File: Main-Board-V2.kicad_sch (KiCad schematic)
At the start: 17 parts, among them IC2 REG1117-5, J1 776280-1, J2 BCS-114-L-S-PE-BE, J3 BCS-114-L-S-PE-BE, J4 776280-1, U4 ADM3057EBRWZ

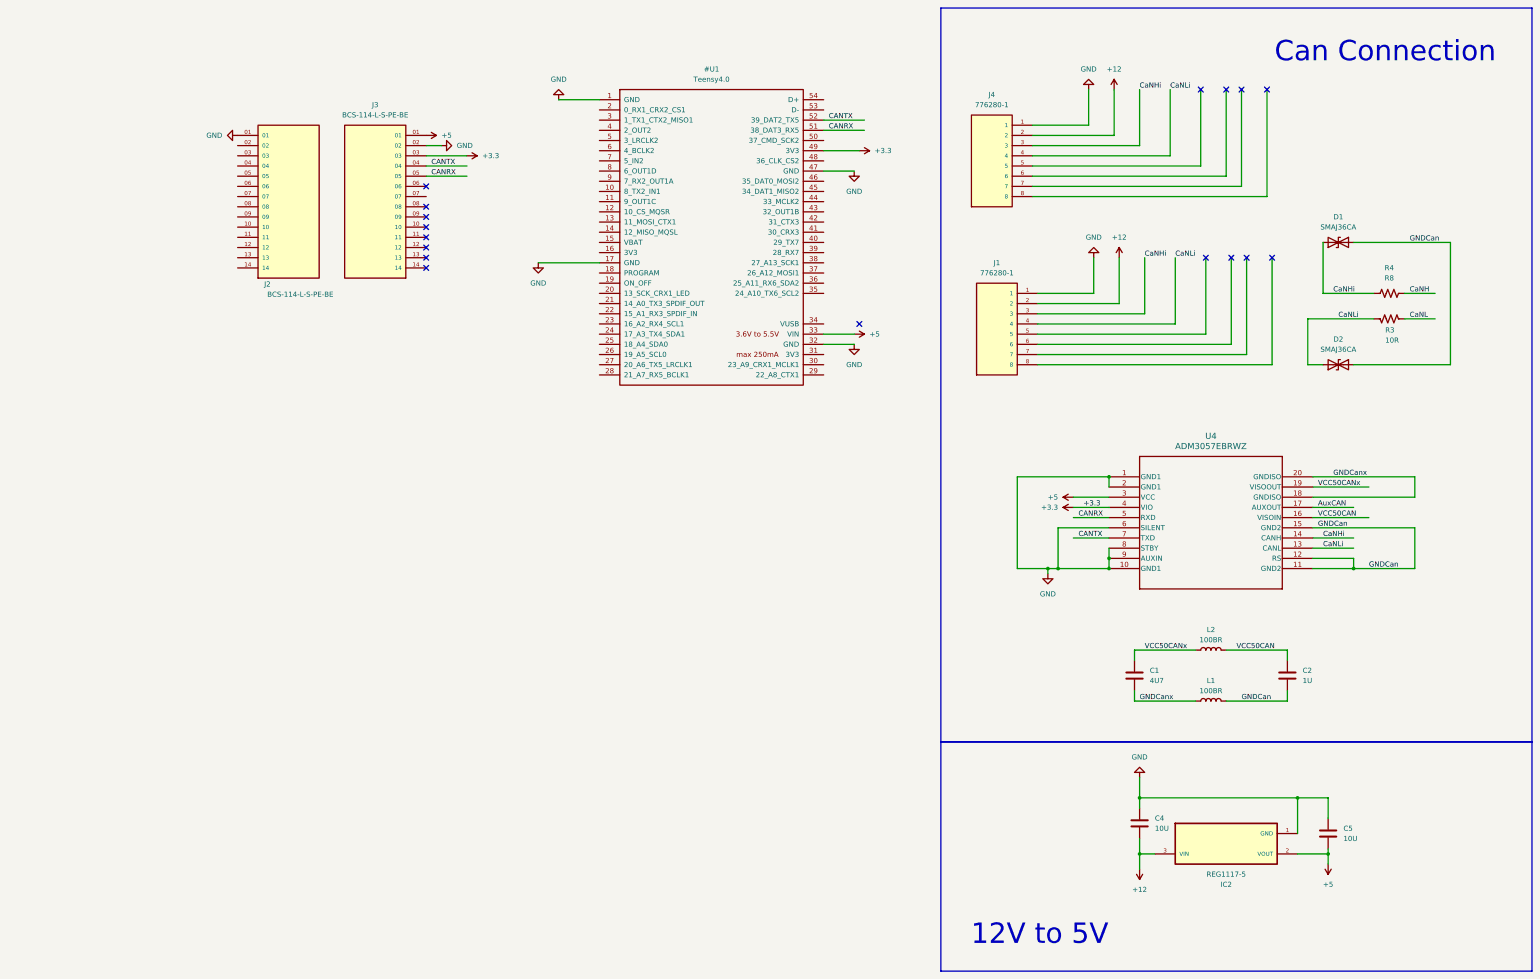
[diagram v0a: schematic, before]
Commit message: Seperated into sub sheets
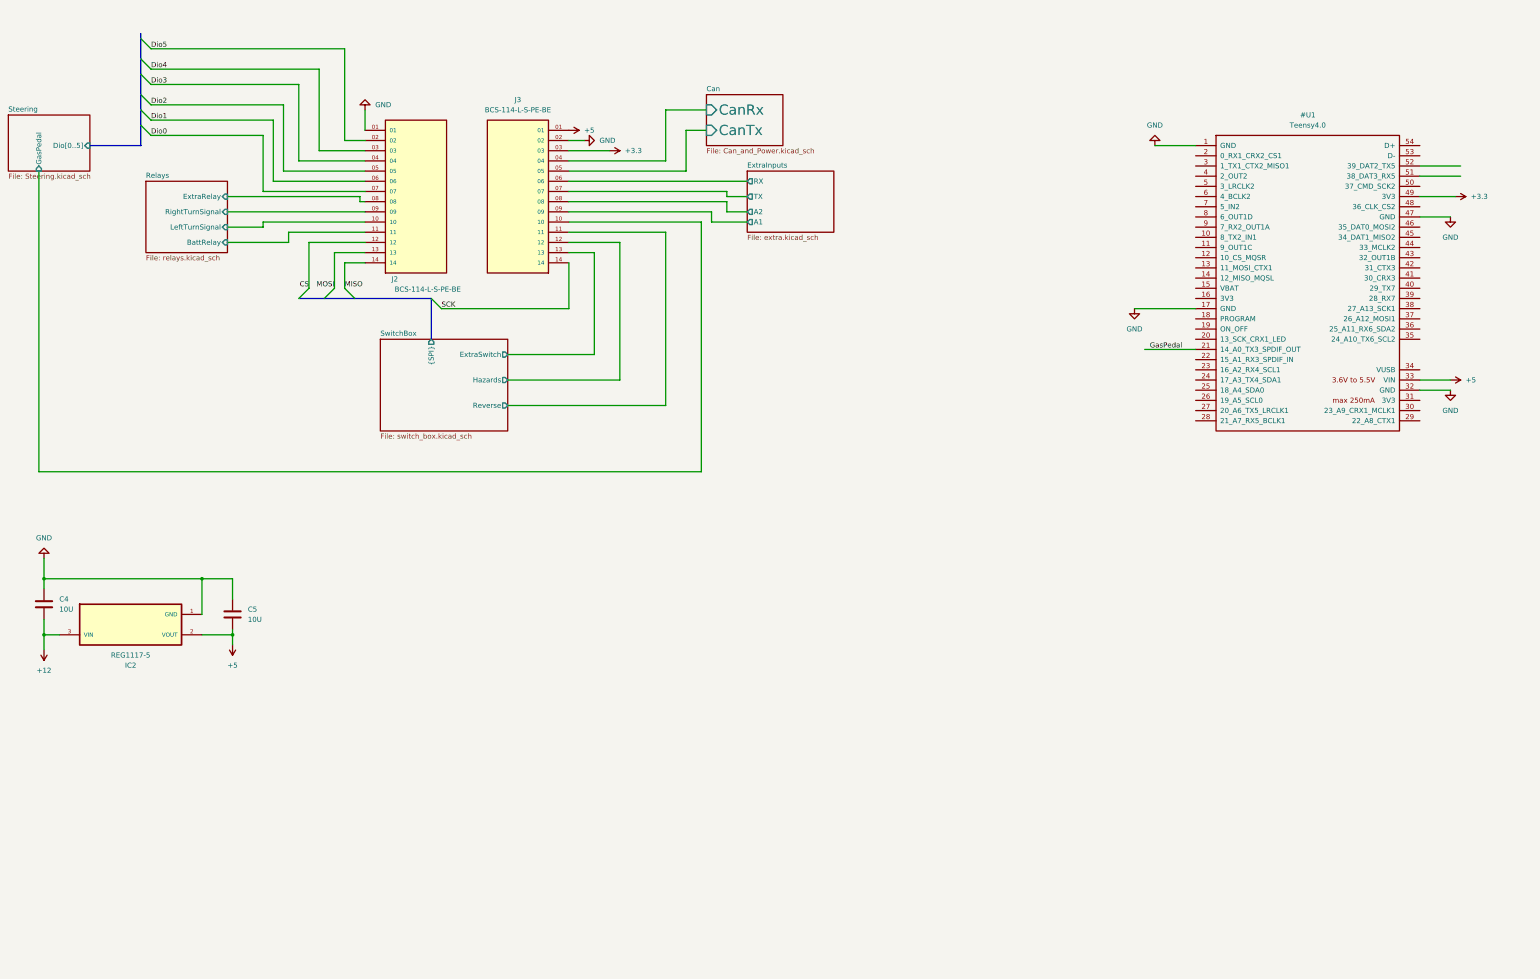
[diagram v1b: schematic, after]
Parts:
- removed C1: 4U7, GRM188R61E475KE11D:CAPC1608X95N, symbol Device:C
- removed C2: 1U, GRT155C80J105KE01J:CAPC1005X55N, symbol Device:C
- removed D1, D2: SMAJ36CA, SMAJ36CA:SMASERIES-M, symbol Diode:SMAJ36CA
- removed J1, J4: 776280-1, 776280-1:TE_776280-1, symbol 776280-1:776280-1
- removed L1, L2: 100BR, RN73C2B100RBTDF:RESC3015X65N, symbol Device:L
- removed R3: 10R, Resistor_SMD:R_0603_1608Metric, symbol Device:R_US
- removed R4: R8, Resistor_SMD:R_0603_1608Metric, symbol Device:R_US
- removed U4: ADM3057EBRWZ, ADM3057EBRWZ:SOIC127P1032X265-20N, symbol 2025-07-12_07-19-05:ADM3057EBRWZ
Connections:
- net Dio5: now reaches J2.02
- net Dio4: now reaches J2.03
- net Dio3: now reaches J2.04
- net Dio2: now reaches J2.05
- net Dio1: now reaches J2.06
- net Dio0: now reaches J2.07
- net Relays/ExtraRelay: now reaches J2.08
- net Relays/RightTurnSignal: now reaches J2.09
- net Relays/LeftTurnSignal: now reaches J2.10
- net Relays/BattRelay: now reaches J2.11
- net CS: now reaches J2.12
- net MOSI: now reaches J2.13
- net MISO: now reaches J2.14
- net GasPedal: now reaches #U1.21 (14_A0_TX3_SPDIF_OUT)
- net ExtraInputs/RX: now reaches J3.06
- net ExtraInputs/TX: now reaches J3.07
- net ExtraInputs/A2: now reaches J3.08
- net ExtraInputs/A1: now reaches J3.09
- net Steering/GasPedal: now reaches J3.10
- net SwitchBox/Reverse: now reaches J3.11
- net SwitchBox/Hazards: now reaches J3.12
- net SwitchBox/ExtraSwitch: now reaches J3.13
- net SCK: now reaches J3.14
- net CANRX: no longer names the net of #U1.51 (38_DAT3_RX5)
- net CANRX: no longer J3.05
- net CANTX: no longer names the net of #U1.52 (39_DAT2_TX5)
- net CANTX: no longer J3.04
- new net Can/CanRx: J3.04
- new net Can/CanTx: J3.05
- no-connect marks 17 -> 0
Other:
- added sheet Can (Can_and_Power.kicad_sch)
- added sheet ExtraInputs (extra.kicad_sch)
- added sheet Relays (relays.kicad_sch)
- added sheet Steering (Steering.kicad_sch)
- added sheet SwitchBox (switch_box.kicad_sch)
- note removed: "12V to 5V"
- note removed: "Can Connection"
- moved on the sheet: C4, C5, IC2, J2, J3

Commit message: Digital IO, Relay, and Switchbox changes
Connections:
- net +3.3: no longer J3.03
- net +5: no longer J3.01
- net GND: no longer C4.1
- net CS: no longer names the net of J2.12
- net Dio0 renamed DigitalInputs/Brake
- net Dio1 renamed DigitalInputs/Dio4
- net Dio2 renamed DigitalInputs/Dio3
- net Dio3 renamed DigitalInputs/Dio2
- net Dio4 renamed DigitalInputs/Dio1
- net Dio5 renamed DigitalInputs/Dio0
- net MISO: no longer names the net of J2.14
- net MOSI: no longer names the net of J2.13
- net SCK: no longer names the net of J3.14
- net DigitalInputs/GasPedal renamed AnalogInputs/GasPedal
- new net +3.3V: J3.03
- new net +5V: J3.01
- new net GNDp: C4.1
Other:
- sheet ExtraInputs renamed AnalogInputs
- sheet Steering renamed DigitalInputs
- sheet AnalogInputs ports: added GasPedal; removed none
- sheet DigitalInputs ports: added Brake, Dio0, Dio1, Dio2, Dio3, Dio4; removed Dio[0..5], GasPedal
- sheet SwitchBox ports: added none; removed {SPI}

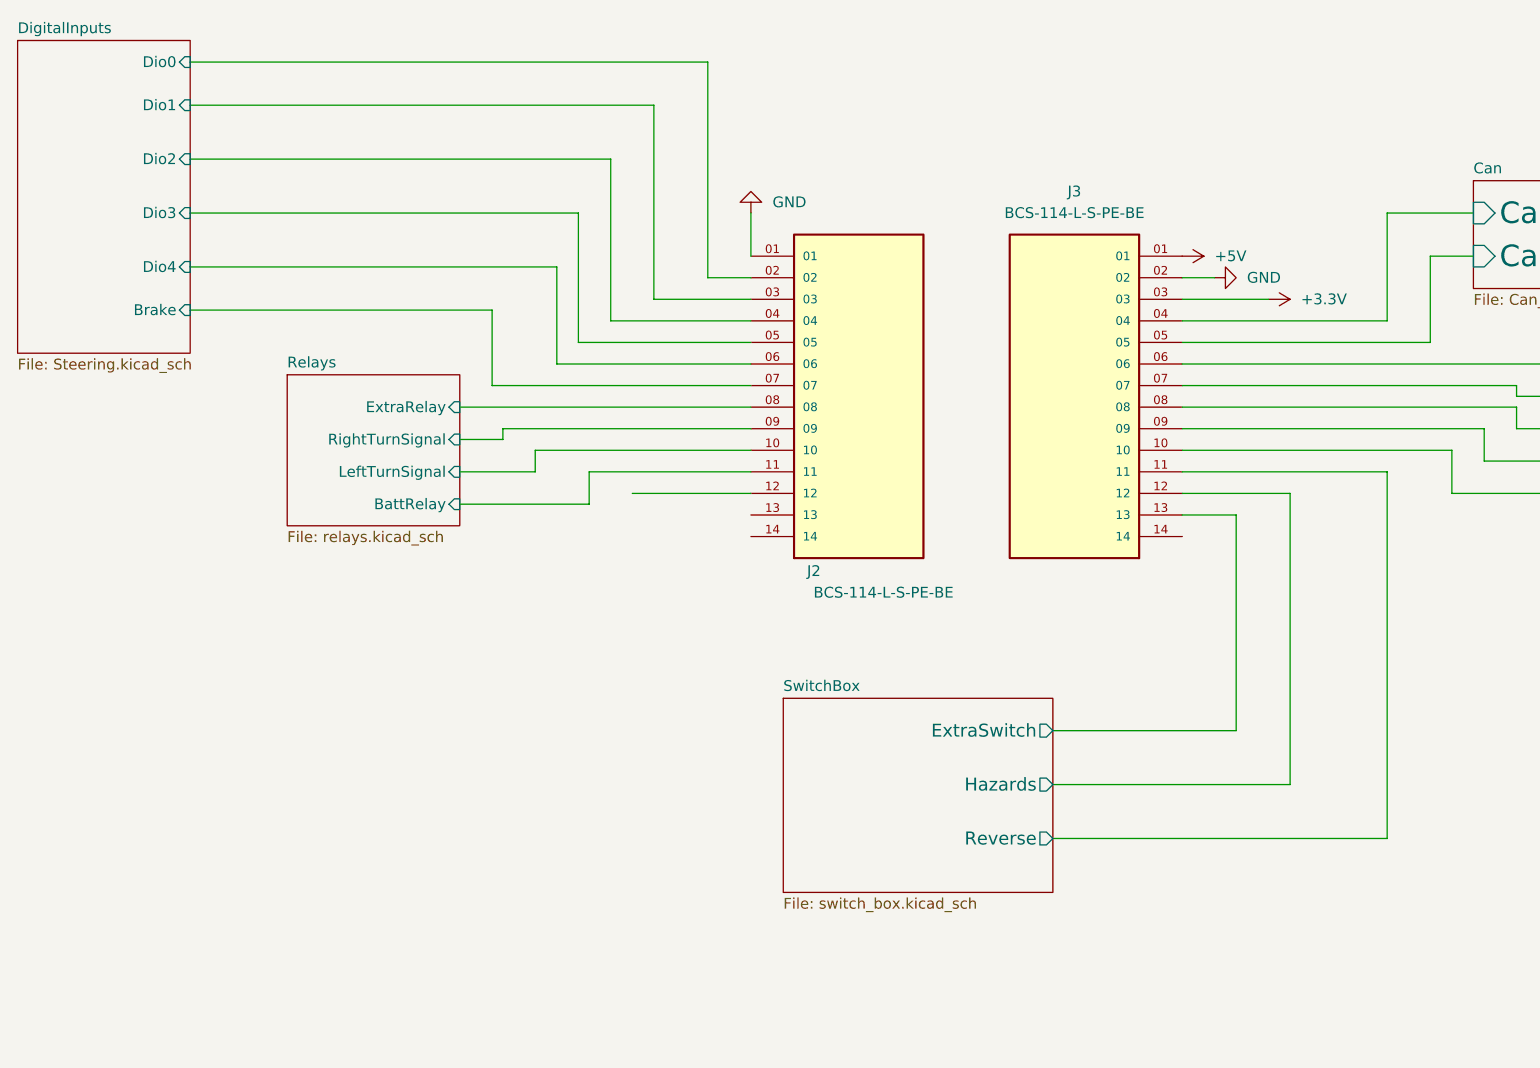
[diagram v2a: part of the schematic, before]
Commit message: Added Analog inputs
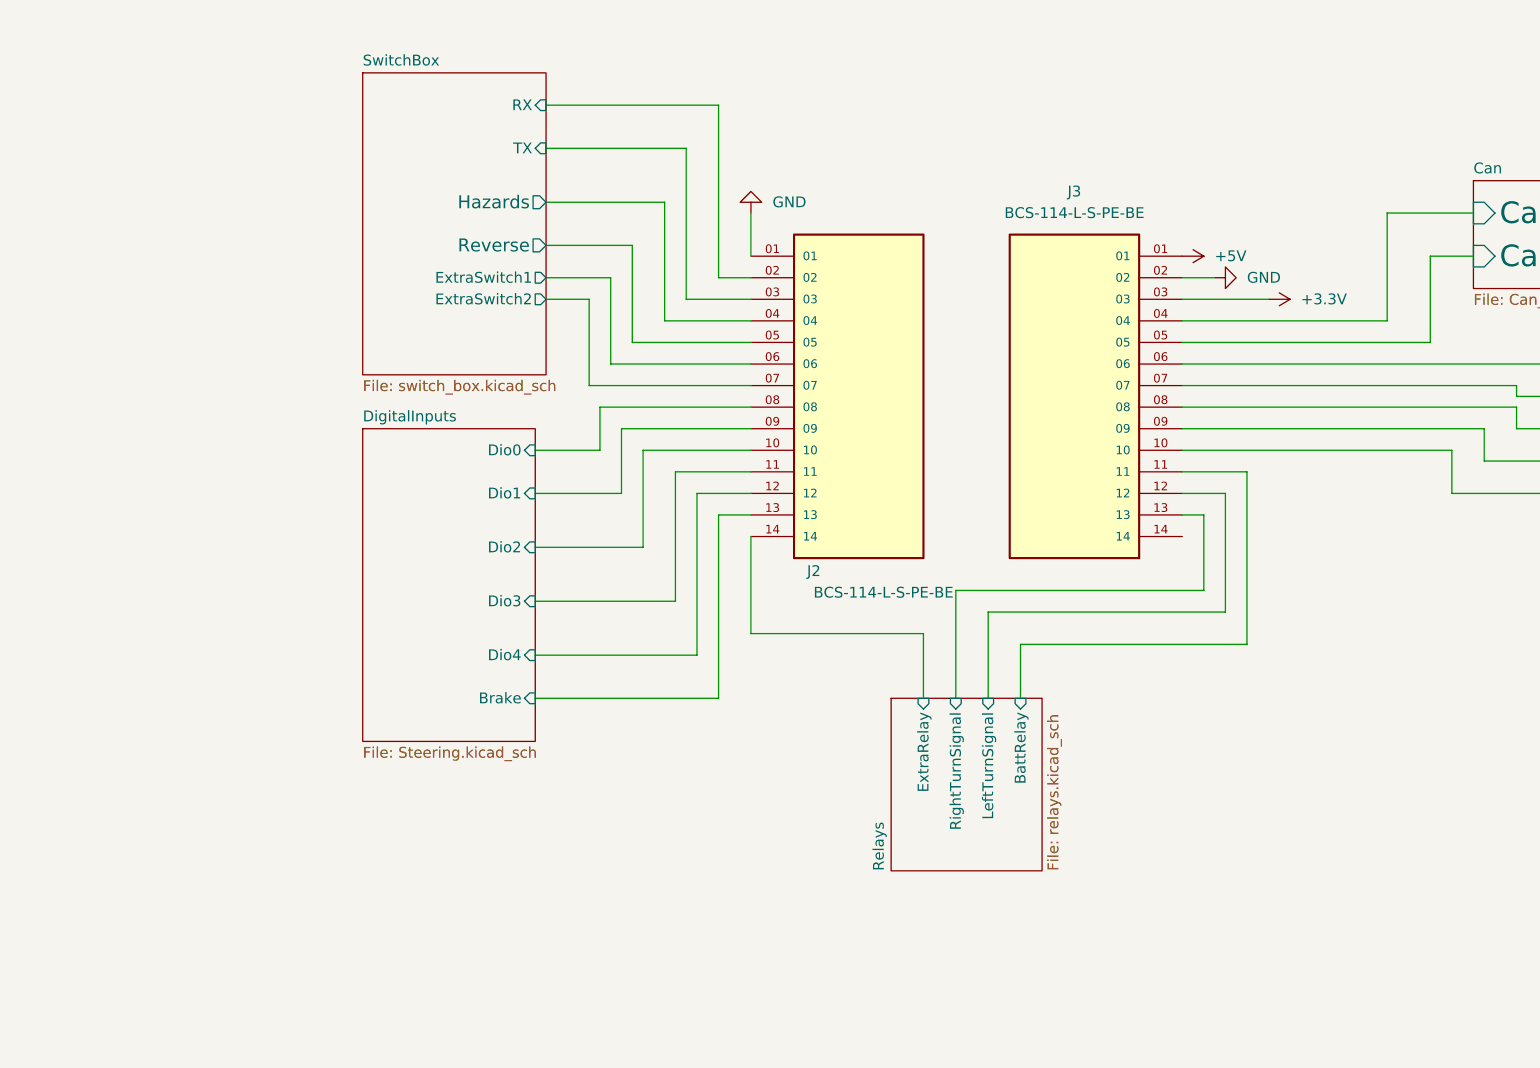
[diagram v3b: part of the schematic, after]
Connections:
- net SwitchBox/ExtraSwitch is gone; now on net Relays/RightTurnSignal: J3.13
- net DigitalInputs/Brake: now also J2.13; no longer J2.07
- net DigitalInputs/Dio0: now also J2.08; no longer J2.02
- net DigitalInputs/Dio1: now also J2.09; no longer J2.03
- net DigitalInputs/Dio2: now also J2.10; no longer J2.04
- net DigitalInputs/Dio3: now also J2.11; no longer J2.05
- net DigitalInputs/Dio4: now also J2.12; no longer J2.06
- net Relays/BattRelay: now also J3.11; no longer J2.11
- net Relays/ExtraRelay: now also J2.14; no longer J2.08
- net Relays/LeftTurnSignal: now also J3.12; no longer J2.10
- net Relays/RightTurnSignal: no longer J2.09
- net SwitchBox/Hazards: now also J2.04; no longer J3.12
- net SwitchBox/Reverse: now also J2.05; no longer J3.11
- new net SwitchBox/ExtraSwitch1: J2.06
- new net SwitchBox/ExtraSwitch2: J2.07
- new net SwitchBox/RX: J2.02
- new net SwitchBox/TX: J2.03
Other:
- sheet SwitchBox ports: added ExtraSwitch1, ExtraSwitch2, RX, TX; removed ExtraSwitch

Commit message: Fixed ERC errors and warnings
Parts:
- removed #U1: Teensy4.0, teensy.pretty-master:Teensy40_SMT, symbol teensy:Teensy4.0
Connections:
- net +5 is gone; now on net +5V: C5.2, IC2.2 (VOUT)
- net +12 renamed +12V
- no-connect marks 0 -> 1

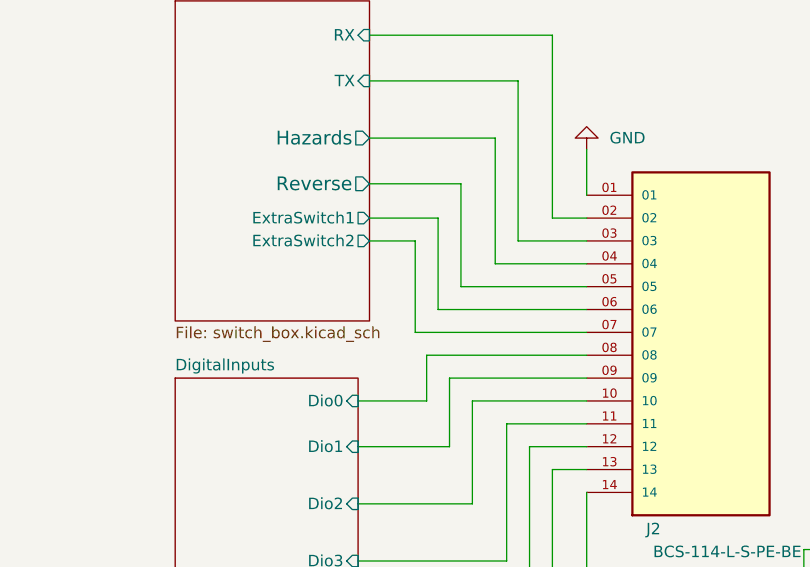
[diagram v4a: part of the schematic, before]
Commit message: Added 5V to switchbox
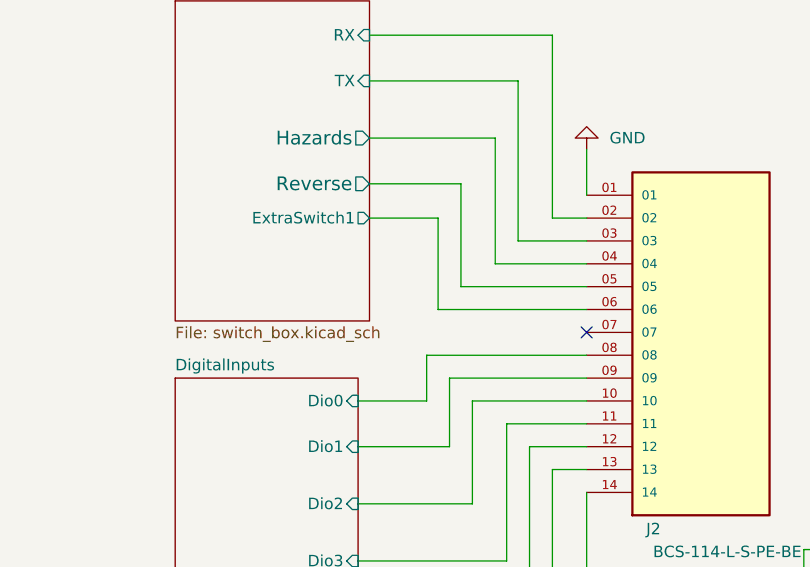
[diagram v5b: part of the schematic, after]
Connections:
- net SwitchBox/ExtraSwitch2: no longer names the net of J2.07
- no-connect marks 1 -> 2
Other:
- sheet SwitchBox ports: added none; removed ExtraSwitch2
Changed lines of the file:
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@@
+	)
+	(no_connect
+		(at 116.84 58.42)
 	)
 	(no_connect
@@
 	(wire
 		(pts
-			(xy 92.71 48.26) (xy 97.79 48.26)
-		)
-		(stroke
-			(width 0)
-			(type default)
-		)
-	)
-	(wire
-		(pts
 			(xy 110.49 71.12) (xy 116.84 71.12)
 		)
@@
 		(pts
 			(xy 140.97 95.25) (xy 140.97 82.55)
-		)
-		(stroke
-			(width 0)
-			(type default)
-		)
-	)
-	(wire
-		(pts
-			(xy 97.79 48.26) (xy 97.79 58.42)
-		)
-		(stroke
-			(width 0)
-			(type default)
-		)
-	)
-	(wire
-		(pts
-			(xy 97.79 58.42) (xy 116.84 58.42)
 		)
 		(stroke
@@
 			(effects
 				(font
-					(size 1.27 1.27)
-				)
-				(justify right)
-			)
-		)
-		(pin "ExtraSwitch2" output
-			(at 92.71 48.26 0)
-			(effects
-				(font
